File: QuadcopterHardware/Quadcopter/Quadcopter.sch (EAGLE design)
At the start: 46 parts, among them J2 FTDI_DEVICERA_SMT, M1 WIRELESS-NRF24L01, U1 ATMEGA328P_TQFP, U3 GY-521MPU6050

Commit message: more updates
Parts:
- removed J1: (no value), SparkFun-Connectors:JST_2MM_MALE
- added U$2: JST_CONNECTOR_FEMALE, quad:JST_CONNECTOR_FEMALE
- RES1: value CSTCE-RESONATOR -> CSTCE10M0G55-R0
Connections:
- net 3V3: now also C9.1; no longer C9.2
- net GND: now also C9.2, U$2.-; no longer C9.1, J1.-
- net VBATT: now also U$2.+; no longer J1.+
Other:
- moved on the sheet: C9, R8, R9

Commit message: more updates
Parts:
- added C14: 100nF, rcl:C-USC0603
- LED4: value GREEN -> RED
- LED5: value YELLOW -> RED
- renumbered LED2 to LED4, LED3 to LED5
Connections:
- net G_LED renamed LED2
- net R_LED renamed LED1
- net Y_LED renamed LED3
- net 3V3: now also C14.1
- net GND: now also C14.2
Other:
- moved on the sheet: C9
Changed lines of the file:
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@@
 <part name="R11" library="rcl" deviceset="R-US_" device="R0603" value="10K"/>
 <part name="LED1" library="led" deviceset="LED" device="CHIP-LED0603" value="RED"/>
-<part name="LED2" library="led" deviceset="LED" device="CHIP-LED0603" value="GREEN"/>
-<part name="LED3" library="led" deviceset="LED" device="CHIP-LED0603" value="YELLOW"/>
 <part name="R1" library="rcl" deviceset="R-US_" device="R0603" value="150"/>
 <part name="R3" library="rcl" deviceset="R-US_" device="R0603" value="150"/>
@@
 <part name="U$2" library="quad" deviceset="JST_CONNECTOR_FEMALE" device=""/>
 <part name="GND13" library="supply1" deviceset="GND" device=""/>
+<part name="C14" library="rcl" deviceset="C-US" device="C0603" value="100nF"/>
+<part name="LED4" library="led" deviceset="LED" device="CHIP-LED0603" value="RED"/>
+<part name="LED5" library="led" deviceset="LED" device="CHIP-LED0603" value="RED"/>
 </parts>
 <sheets>
@@
 <instance part="R11" gate="G$1" x="0" y="-33.02" rot="R90"/>
 <instance part="LED1" gate="G$1" x="-40.64" y="162.56" rot="R90"/>
-<instance part="LED2" gate="G$1" x="-40.64" y="149.86" rot="R90"/>
-<instance part="LED3" gate="G$1" x="-40.64" y="137.16" rot="R90"/>
 <instance part="R1" gate="G$1" x="-25.4" y="162.56"/>
 <instance part="R3" gate="G$1" x="-25.4" y="149.86"/>
@@
 <instance part="GND16" gate="1" x="-127" y="60.96"/>
 <instance part="GND17" gate="1" x="-20.32" y="127"/>
-<instance part="C9" gate="G$1" x="-218.44" y="71.12" rot="R180"/>
+<instance part="C9" gate="G$1" x="-231.14" y="71.12" rot="R180"/>
 <instance part="C8" gate="G$1" x="-248.92" y="132.08" rot="R270"/>
 <instance part="C10" gate="G$1" x="-162.56" y="-7.62"/>
@@
 <instance part="U$2" gate="G$1" x="-241.3" y="154.94" rot="R180"/>
 <instance part="GND13" gate="1" x="-182.88" y="109.22"/>
+<instance part="C14" gate="G$1" x="-215.9" y="71.12" rot="R180"/>
+<instance part="LED4" gate="G$1" x="-40.64" y="149.86" rot="R90"/>
+<instance part="LED5" gate="G$1" x="-40.64" y="137.16" rot="R90"/>
 </instances>
 <busses>
@@
 <pinref part="C9" gate="G$1" pin="2"/>
 <wire x1="-210.82" y1="76.2" x2="-210.82" y2="71.12" width="0.1524" layer="91"/>
-<wire x1="-218.44" y1="76.2" x2="-210.82" y2="76.2" width="0.1524" layer="91"/>
+<wire x1="-231.14" y1="76.2" x2="-215.9" y2="76.2" width="0.1524" layer="91"/>
 <junction x="-210.82" y="76.2"/>
+<pinref part="C14" gate="G$1" pin="2"/>
+<wire x1="-215.9" y1="76.2" x2="-210.82" y2="76.2" width="0.1524" layer="91"/>
+<junction x="-215.9" y="76.2"/>
 </segment>
 <segment>
@@
 <wire x1="-104.14" y1="99.06" x2="-139.7" y2="99.06" width="0.1524" layer="91"/>
 <label x="-139.7" y="99.06" size="1.778" layer="95" rot="R180" xref="yes"/>
+</segment>
+<segment>
+<pinref part="U3" gate="G$1" pin="VCC"/>
+<wire x1="17.78" y1="119.38" x2="12.7" y2="119.38" width="0.1524" layer="91"/>
+<label x="12.7" y="119.38" size="1.778" layer="95" rot="R180" xref="yes"/>
+</segment>
+<segment>
+<pinref part="J2" gate="G$1" pin="VCC"/>
+<wire x1="60.96" y1="53.34" x2="55.88" y2="53.34" width="0.1524" layer="91"/>
+<label x="55.88" y="53.34" size="1.778" layer="95" rot="R180" xref="yes"/>
+</segment>
+<segment>
+<pinref part="M1" gate="G$1" pin="VCC"/>
+<pinref part="C9" gate="G$1" pin="1"/>
+<wire x1="-210.82" y1="68.58" x2="-215.9" y2="68.58" width="0.1524" layer="91"/>
+<wire x1="-215.9" y1="68.58" x2="-231.14" y2="68.58" width="0.1524" layer="91"/>
+<wire x1="-231.14" y1="68.58" x2="-246.38" y2="68.58" width="0.1524" layer="91"/>
+<junction x="-231.14" y="68.58"/>
+<label x="-246.38" y="68.58" size="1.778" layer="95" rot="R180" xref="yes"/>
+<pinref part="C14" gate="G$1" pin="1"/>
+<junction x="-215.9" y="68.58"/>
+</segment>
+<segment>
 <pinref part="U1" gate="U$1" pin="VCC@6"/>
 <pinref part="C5" gate="G$1" pin="1"/>
 <wire x1="-129.54" y1="93.98" x2="-129.54" y2="96.52" width="0.1524" layer="91"/>
 <wire x1="-129.54" y1="96.52" x2="-104.14" y2="96.52" width="0.1524" layer="91"/>
-<wire x1="-104.14" y1="96.52" x2="-104.14" y2="99.06" width="0.1524" layer="91"/>
-<junction x="-104.14" y="96.52"/>
-<junction x="-104.14" y="99.06"/>
+<label x="-129.54" y="96.52" size="1.778" layer="95" rot="R180" xref="yes"/>
+</segment>
+<segment>
+<pinref part="U1" gate="U$1" pin="AVCC"/>
 <pinref part="C3" gate="G$1" pin="1"/>
 <wire x1="-149.86" y1="93.98" x2="-149.86" y2="101.6" width="0.1524" layer="91"/>
-<pinref part="U1" gate="U$1" pin="AVCC"/>
 <wire x1="-149.86" y1="101.6" x2="-104.14" y2="101.6" width="0.1524" layer="91"/>
 <label x="-149.86" y="96.52" size="1.778" layer="95" rot="R180" xref="yes"/>
-<wire x1="-104.14" y1="99.06" x2="-104.14" y2="101.6" width="0.1524" layer="91"/>
-<junction x="-104.14" y="101.6"/>
-</segment>
-<segment>
-<pinref part="U3" gate="G$1" pin="VCC"/>
-<wire x1="17.78" y1="119.38" x2="12.7" y2="119.38" width="0.1524" layer="91"/>
-<label x="12.7" y="119.38" size="1.778" layer="95" rot="R180" xref="yes"/>
-</segment>
-<segment>
-<pinref part="J2" gate="G$1" pin="VCC"/>
-<wire x1="60.96" y1="53.34" x2="55.88" y2="53.34" width="0.1524" layer="91"/>
-<label x="55.88" y="53.34" size="1.778" layer="95" rot="R180" xref="yes"/>
-</segment>
-<segment>
-<pinref part="M1" gate="G$1" pin="VCC"/>
-<pinref part="C9" gate="G$1" pin="1"/>
-<wire x1="-210.82" y1="68.58" x2="-218.44" y2="68.58" width="0.1524" layer="91"/>
-<wire x1="-218.44" y1="68.58" x2="-246.38" y2="68.58" width="0.1524" layer="91"/>
-<junction x="-218.44" y="68.58"/>
-<label x="-246.38" y="68.58" size="1.778" layer="95" rot="R180" xref="yes"/>
 </segment>
 </net>
@@
 </segment>
 </net>
-<net name="R_LED" class="0">
+<net name="N$3" class="0">
+<segment>
+<pinref part="R4" gate="G$1" pin="1"/>
+<wire x1="-35.56" y1="137.16" x2="-30.48" y2="137.16" width="0.1524" layer="91"/>
+<pinref part="LED5" gate="G$1" pin="C"/>
+</segment>
+</net>
+<net name="N$5" class="0">
+<segment>
+<pinref part="LED1" gate="G$1" pin="C"/>
+<pinref part="R1" gate="G$1" pin="1"/>
+<wire x1="-35.56" y1="162.56" x2="-30.48" y2="162.56" width="0.1524" layer="91"/>
+</segment>
+</net>
+<net name="N$2" class="0">
+<segment>
+<pinref part="LED4" gate="G$1" pin="C"/>
+<pinref part="R3" gate="G$1" pin="1"/>
+<wire x1="-35.56" y1="149.86" x2="-30.48" y2="149.86" width="0.1524" layer="91"/>
+</segment>
+</net>
+<net name="LED2" class="0">
+<segment>
+<wire x1="-43.18" y1="149.86" x2="-55.88" y2="149.86" width="0.1524" layer="91"/>
+<label x="-55.88" y="149.86" size="1.778" layer="95" rot="R180" xref="yes"/>
+<pinref part="LED4" gate="G$1" pin="A"/>
+</segment>
+<segment>
+<pinref part="U1" gate="U$1" pin="PC2(ADC2)"/>
+<wire x1="-55.88" y1="101.6" x2="-50.8" y2="101.6" width="0.1524" layer="91"/>
+<label x="-50.8" y="101.6" size="1.778" layer="95" xref="yes"/>
+</segment>
+</net>
+<net name="LED1" class="0">
 <segment>
 <pinref part="LED1" gate="G$1" pin="A"/>
@@
 </segment>
 </net>
-<net name="G_LED" class="0">
-<segment>
-<pinref part="LED2" gate="G$1" pin="A"/>
-<wire x1="-43.18" y1="149.86" x2="-55.88" y2="149.86" width="0.1524" layer="91"/>
-<label x="-55.88" y="149.86" size="1.778" layer="95" rot="R180" xref="yes"/>
-</segment>
-<segment>
-<pinref part="U1" gate="U$1" pin="PC2(ADC2)"/>
-<wire x1="-55.88" y1="101.6" x2="-50.8" y2="101.6" width="0.1524" layer="91"/>
-<label x="-50.8" y="101.6" size="1.778" layer="95" xref="yes"/>
-</segment>
-</net>
-<net name="Y_LED" class="0">
-<segment>
-<pinref part="LED3" gate="G$1" pin="A"/>
+<net name="LED3" class="0">
+<segment>
 <wire x1="-43.18" y1="137.16" x2="-55.88" y2="137.16" width="0.1524" layer="91"/>
 <label x="-55.88" y="137.16" size="1.778" layer="95" rot="R180" xref="yes"/>
+<pinref part="LED5" gate="G$1" pin="A"/>
 </segment>
 <segment>
@@
 </segment>
 </net>
-<net name="N$3" class="0">
-<segment>
-<pinref part="LED3" gate="G$1" pin="C"/>
-<pinref part="R4" gate="G$1" pin="1"/>
-<wire x1="-35.56" y1="137.16" x2="-30.48" y2="137.16" width="0.1524" layer="91"/>
-</segment>
-</net>
-<net name="N$4" class="0">
-<segment>
-<pinref part="LED2" gate="G$1" pin="C"/>
-<pinref part="R3" gate="G$1" pin="1"/>
-<wire x1="-35.56" y1="149.86" x2="-30.48" y2="149.86" width="0.1524" layer="91"/>
-</segment>
-</net>
-<net name="N$5" class="0">
-<segment>
-<pinref part="LED1" gate="G$1" pin="C"/>
-<pinref part="R1" gate="G$1" pin="1"/>
-<wire x1="-35.56" y1="162.56" x2="-30.48" y2="162.56" width="0.1524" layer="91"/>
-</segment>
-</net>

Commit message: more updates, generated board
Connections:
- new net N$4: U1.PD2(INT0), U3.INT
- net CE: now also U1.PB0(ICP); no longer U1.PD2(INT0)
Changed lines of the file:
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@@
 <instance part="C5" gate="G$1" x="-129.54" y="91.44"/>
 <instance part="U3" gate="G$1" x="33.02" y="104.14"/>
-<instance part="GND14" gate="1" x="5.08" y="73.66"/>
+<instance part="GND14" gate="1" x="5.08" y="88.9"/>
 <instance part="J2" gate="G$1" x="66.04" y="55.88"/>
 <instance part="GND15" gate="1" x="60.96" y="43.18"/>
@@
 <segment>
 <pinref part="GND14" gate="1" pin="GND"/>
-<wire x1="5.08" y1="76.2" x2="5.08" y2="114.3" width="0.1524" layer="91"/>
+<wire x1="5.08" y1="91.44" x2="5.08" y2="114.3" width="0.1524" layer="91"/>
 <pinref part="U3" gate="G$1" pin="GND"/>
 <wire x1="5.08" y1="114.3" x2="17.78" y2="114.3" width="0.1524" layer="91"/>
@@
 </segment>
 <segment>
-<pinref part="U1" gate="U$1" pin="PD2(INT0)"/>
-<wire x1="-55.88" y1="78.74" x2="-22.86" y2="78.74" width="0.1524" layer="91"/>
-<label x="-22.86" y="78.74" size="1.778" layer="95" xref="yes"/>
+<pinref part="U1" gate="U$1" pin="PB0(ICP)"/>
+<wire x1="-55.88" y1="60.96" x2="-30.48" y2="60.96" width="0.1524" layer="91"/>
+<label x="-30.48" y="60.96" size="1.778" layer="95" xref="yes"/>
 </segment>
 </net>
@@
 </segment>
 </net>
+<net name="N$4" class="0">
+<segment>
+<pinref part="U1" gate="U$1" pin="PD2(INT0)"/>
+<pinref part="U3" gate="G$1" pin="INT"/>
+<wire x1="-55.88" y1="78.74" x2="17.78" y2="78.74" width="0.1524" layer="91"/>
+<wire x1="17.78" y1="78.74" x2="17.78" y2="83.82" width="0.1524" layer="91"/>
+</segment>
+</net>

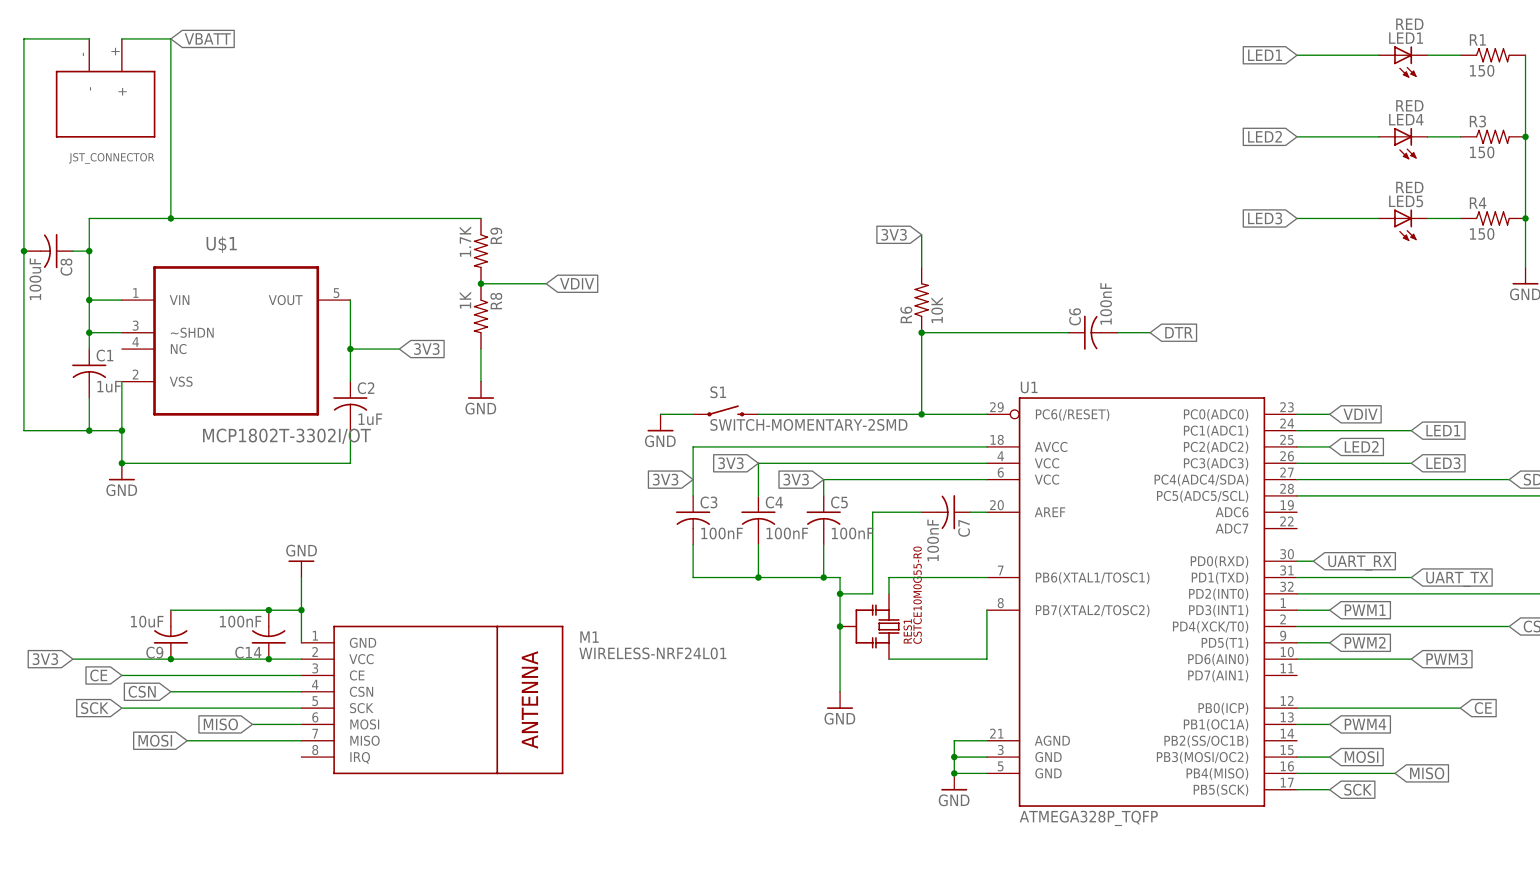
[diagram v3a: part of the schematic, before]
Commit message: started working on the board...fixed errors in schematic
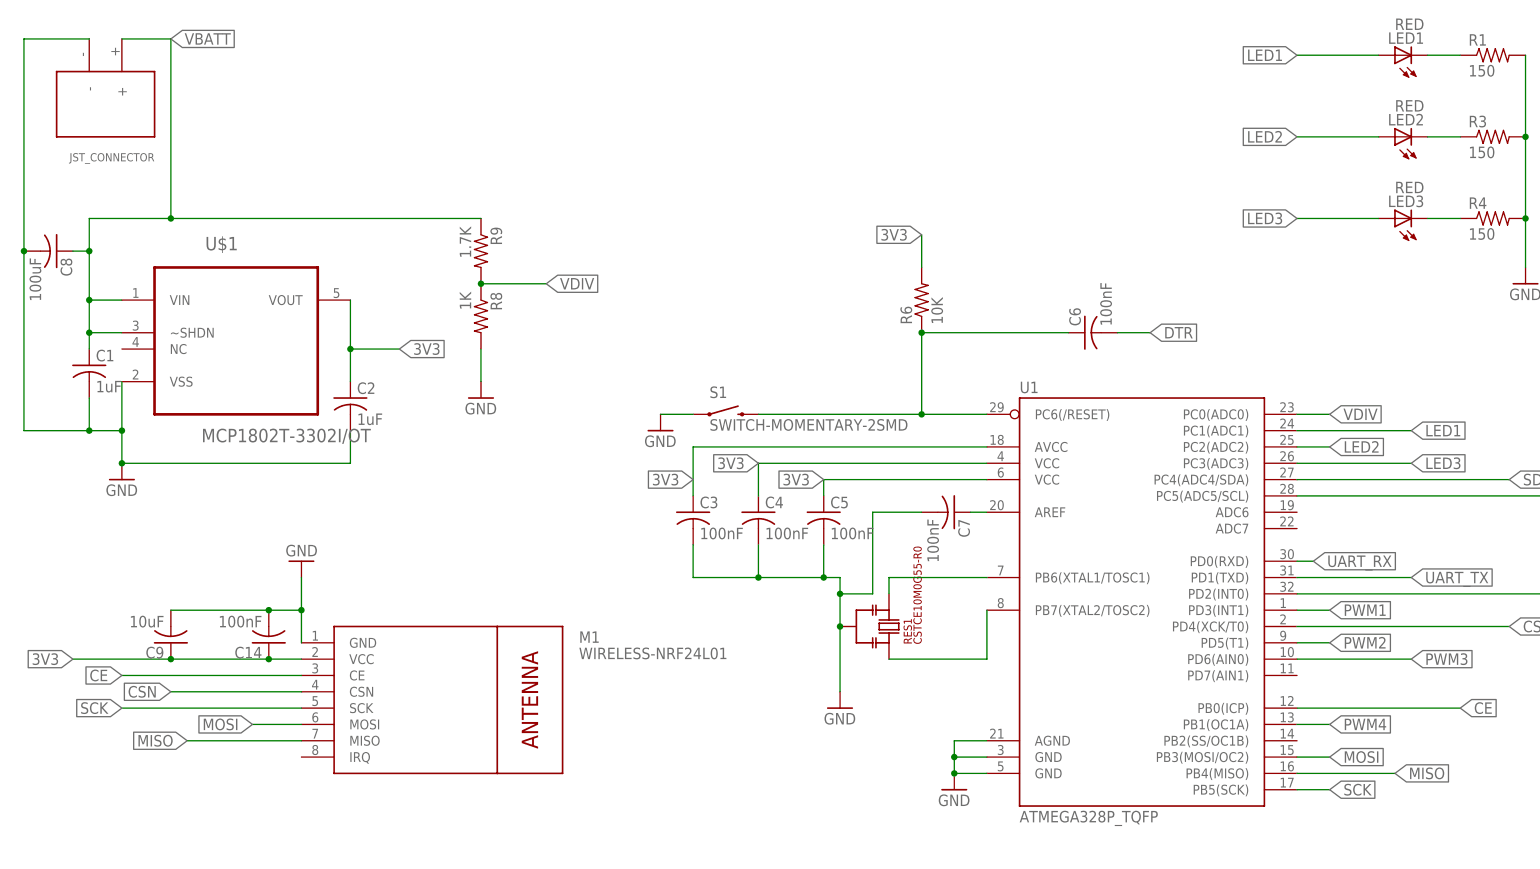
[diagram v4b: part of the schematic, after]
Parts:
- U$2: value JST_CONNECTOR_FEMALE -> JST_Battery
- renumbered LED4 to LED2, LED5 to LED3
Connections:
- net N$1 renamed AREF
- net N$4 renamed ACC_INT
- net MISO: now also M1.MISO; no longer M1.MOSI
- net MOSI: now also M1.MOSI; no longer M1.MISO
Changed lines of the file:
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@@
 <part name="C12" library="rcl" deviceset="C-US" device="C1206" value="100uF"/>
 <part name="C13" library="rcl" deviceset="C-US" device="C1206" value="100uF"/>
-<part name="U$2" library="quad" deviceset="JST_CONNECTOR_FEMALE" device=""/>
+<part name="U$2" library="quad" deviceset="JST_CONNECTOR_FEMALE" device="" value="JST_Battery"/>
 <part name="GND13" library="supply1" deviceset="GND" device=""/>
 <part name="C14" library="rcl" deviceset="C-US" device="C0603" value="100nF"/>
-<part name="LED4" library="led" deviceset="LED" device="CHIP-LED0603" value="RED"/>
-<part name="LED5" library="led" deviceset="LED" device="CHIP-LED0603" value="RED"/>
+<part name="LED2" library="led" deviceset="LED" device="CHIP-LED0603" value="RED"/>
+<part name="LED3" library="led" deviceset="LED" device="CHIP-LED0603" value="RED"/>
 </parts>
 <sheets>
@@
 <instance part="GND13" gate="1" x="-182.88" y="109.22"/>
 <instance part="C14" gate="G$1" x="-215.9" y="71.12" rot="R180"/>
-<instance part="LED4" gate="G$1" x="-40.64" y="149.86" rot="R90"/>
-<instance part="LED5" gate="G$1" x="-40.64" y="137.16" rot="R90"/>
+<instance part="LED2" gate="G$1" x="-40.64" y="149.86" rot="R90"/>
+<instance part="LED3" gate="G$1" x="-40.64" y="137.16" rot="R90"/>
 </instances>
 <busses>
@@
 </segment>
 <segment>
+<pinref part="M1" gate="G$1" pin="MISO"/>
+<wire x1="-210.82" y1="55.88" x2="-228.6" y2="55.88" width="0.1524" layer="91"/>
+<label x="-228.6" y="55.88" size="1.778" layer="95" rot="R180" xref="yes"/>
+</segment>
+</net>
+<net name="SCK" class="0">
+<segment>
+<pinref part="U1" gate="U$1" pin="PB5(SCK)"/>
+<wire x1="-55.88" y1="48.26" x2="-50.8" y2="48.26" width="0.1524" layer="91"/>
+<label x="-50.8" y="48.26" size="1.778" layer="95" xref="yes"/>
+</segment>
+<segment>
+<pinref part="M1" gate="G$1" pin="SCK"/>
+<wire x1="-210.82" y1="60.96" x2="-238.76" y2="60.96" width="0.1524" layer="91"/>
+<label x="-238.76" y="60.96" size="1.778" layer="95" rot="R180" xref="yes"/>
+</segment>
+</net>
+<net name="MOSI" class="0">
+<segment>
+<pinref part="U1" gate="U$1" pin="PB3(MOSI/OC2)"/>
+<label x="-50.8" y="53.34" size="1.778" layer="95" xref="yes"/>
+<wire x1="-55.88" y1="53.34" x2="-50.8" y2="53.34" width="0.1524" layer="91"/>
+</segment>
+<segment>
 <pinref part="M1" gate="G$1" pin="MOSI"/>
 <wire x1="-210.82" y1="58.42" x2="-218.44" y2="58.42" width="0.1524" layer="91"/>
 <label x="-218.44" y="58.42" size="1.778" layer="95" rot="R180" xref="yes"/>
-</segment>
-</net>
-<net name="SCK" class="0">
-<segment>
-<pinref part="U1" gate="U$1" pin="PB5(SCK)"/>
-<wire x1="-55.88" y1="48.26" x2="-50.8" y2="48.26" width="0.1524" layer="91"/>
-<label x="-50.8" y="48.26" size="1.778" layer="95" xref="yes"/>
-</segment>
-<segment>
-<pinref part="M1" gate="G$1" pin="SCK"/>
-<wire x1="-210.82" y1="60.96" x2="-238.76" y2="60.96" width="0.1524" layer="91"/>
-<label x="-238.76" y="60.96" size="1.778" layer="95" rot="R180" xref="yes"/>
-</segment>
-</net>
-<net name="MOSI" class="0">
-<segment>
-<pinref part="U1" gate="U$1" pin="PB3(MOSI/OC2)"/>
-<label x="-50.8" y="53.34" size="1.778" layer="95" xref="yes"/>
-<wire x1="-55.88" y1="53.34" x2="-50.8" y2="53.34" width="0.1524" layer="91"/>
-</segment>
-<segment>
-<pinref part="M1" gate="G$1" pin="MISO"/>
-<wire x1="-210.82" y1="55.88" x2="-228.6" y2="55.88" width="0.1524" layer="91"/>
-<label x="-228.6" y="55.88" size="1.778" layer="95" rot="R180" xref="yes"/>
 </segment>
 </net>
@@
 </segment>
 </net>
-<net name="N$1" class="0">
+<net name="AREF" class="0">
 <segment>
 <pinref part="U1" gate="U$1" pin="AREF"/>
@@
 <pinref part="R4" gate="G$1" pin="1"/>
 <wire x1="-35.56" y1="137.16" x2="-30.48" y2="137.16" width="0.1524" layer="91"/>
-<pinref part="LED5" gate="G$1" pin="C"/>
+<pinref part="LED3" gate="G$1" pin="C"/>
 </segment>
 </net>
@@
 <net name="N$2" class="0">
 <segment>
-<pinref part="LED4" gate="G$1" pin="C"/>
+<pinref part="LED2" gate="G$1" pin="C"/>
 <pinref part="R3" gate="G$1" pin="1"/>
 <wire x1="-35.56" y1="149.86" x2="-30.48" y2="149.86" width="0.1524" layer="91"/>
@@
 <wire x1="-43.18" y1="149.86" x2="-55.88" y2="149.86" width="0.1524" layer="91"/>
 <label x="-55.88" y="149.86" size="1.778" layer="95" rot="R180" xref="yes"/>
-<pinref part="LED4" gate="G$1" pin="A"/>
+<pinref part="LED2" gate="G$1" pin="A"/>
 </segment>
 <segment>
@@
 <wire x1="-43.18" y1="137.16" x2="-55.88" y2="137.16" width="0.1524" layer="91"/>
 <label x="-55.88" y="137.16" size="1.778" layer="95" rot="R180" xref="yes"/>
-<pinref part="LED5" gate="G$1" pin="A"/>
+<pinref part="LED3" gate="G$1" pin="A"/>
 </segment>
 <segment>
@@
 </segment>
 </net>
-<net name="N$4" class="0">
+<net name="ACC_INT" class="0">
 <segment>
 <pinref part="U1" gate="U$1" pin="PD2(INT0)"/>
